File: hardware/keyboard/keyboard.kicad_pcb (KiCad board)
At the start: 2 copper layers, 234.9 x 95.7 mm, 82 parts, among them J1 Conn_01x02_Female, J2 Conn_01x03_Female, Q1 Q_NMOS_SGD, SW1 SW_Push, U1 SC0915, U10 CherryMX_LED, U11 CherryMX_LED, U12 CherryMX_LED, U13 CherryMX_LED, U14 CherryMX_LED, U15 CherryMX_LED, U16 CherryMX_LED, U17 CherryMX_LED, U18 CherryMX_LED, U19 CherryMX_LED, U2 MCP23008-xP, U20 CherryMX_LED, U21 CherryMX_LED, U22 CherryMX_LED, U23 CherryMX_LED, U24 CherryMX_LED, U25 CherryMX_LED, U26 CherryMX_LED, U27 CherryMX_LED, U28 CherryMX_LED, U29 CherryMX_LED, U3 CherryMX_LED, U30 CherryMX_LED, U31 CherryMX_LED, U32 CherryMX_LED, U33 CherryMX_LED, U34 CherryMX_LED, U35 CherryMX_LED, U36 CherryMX_LED, U4 CherryMX_LED, U5 CherryMX_LED, U6 CherryMX_LED, U7 CherryMX_LED, U8 CherryMX_LED, U9 CherryMX_LED

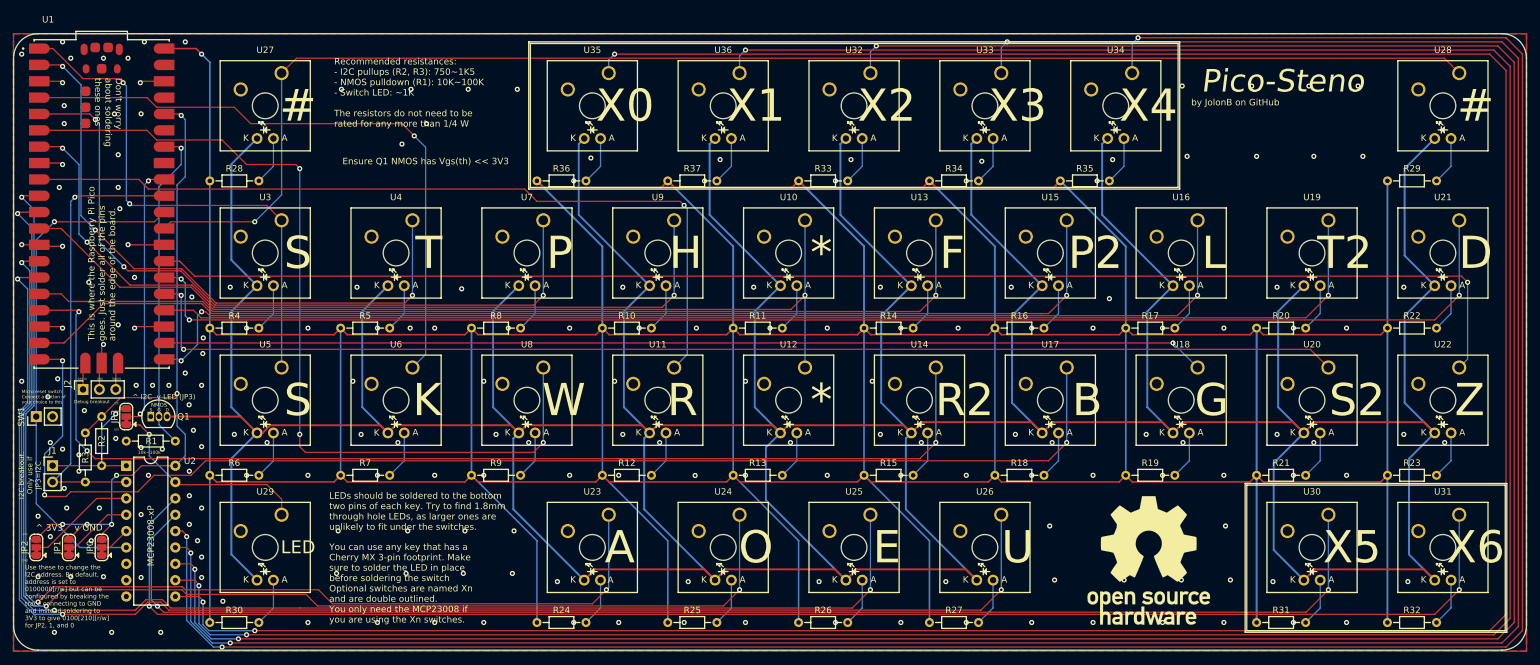
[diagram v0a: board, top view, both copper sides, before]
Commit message: Update I2C header
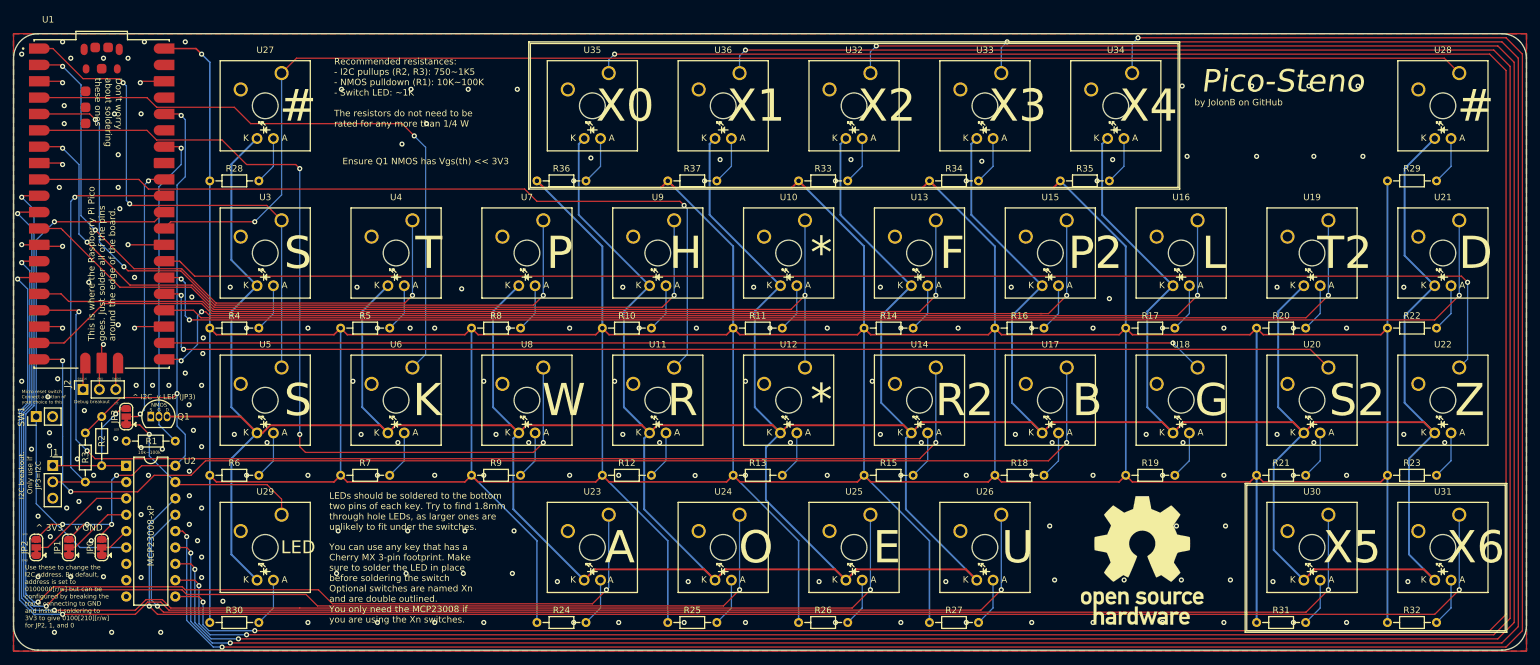
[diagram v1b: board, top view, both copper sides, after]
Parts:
- J1: value Conn_01x02_Female -> Conn_01x03_Female; footprint Connector_PinHeader_2.54mm:PinHeader_1x02_P2.54mm_Vertical -> Connector_PinSocket_2.54mm:PinSocket_1x03_P2.54mm_Vertical
- moved REF** 1.02 mm to (251.5, 215.1)
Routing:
- net /KEY_B: track 199.7 -> 194.1 mm
- net GND: vias 206 -> 207

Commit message: Add mounting holes
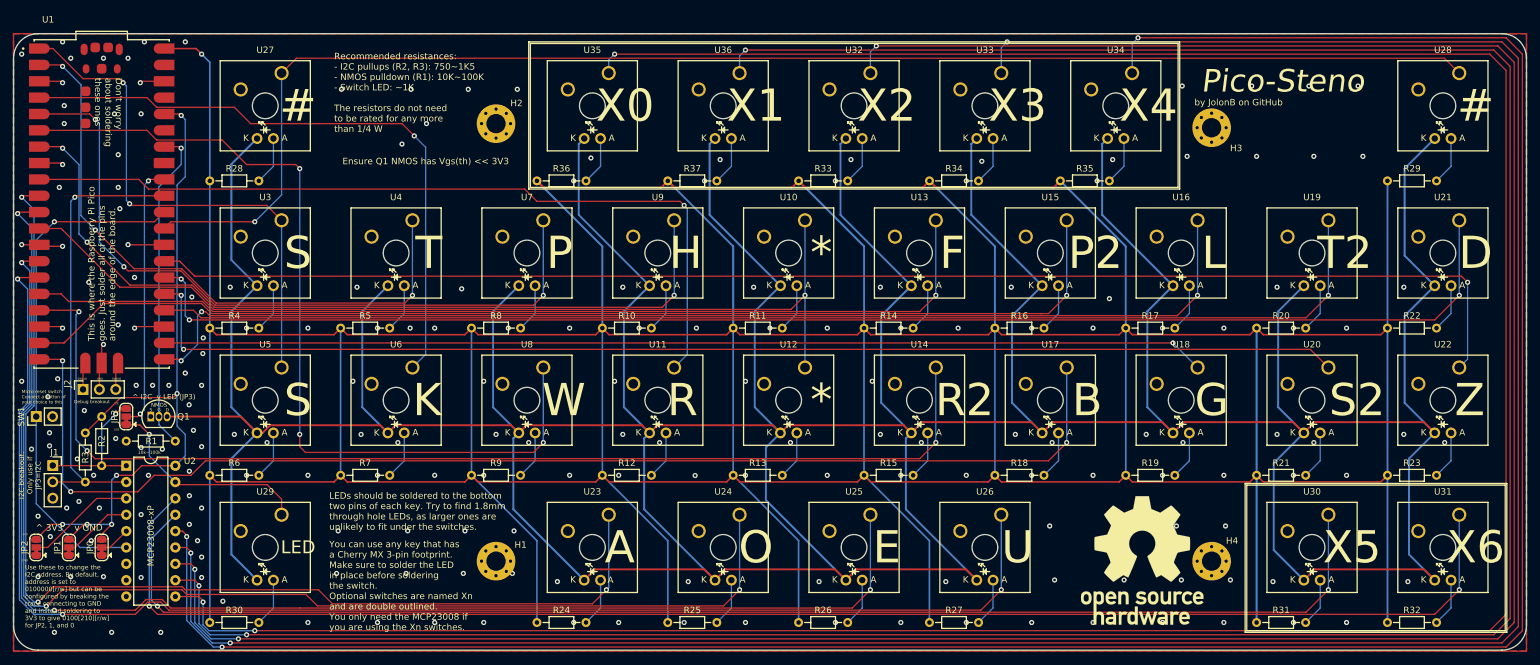
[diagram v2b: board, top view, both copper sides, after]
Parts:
- added H1: MountingHole_Pad, MountingHole:MountingHole_3mm_Pad_Via, F.Cu at (151.1, 215.3)
- added H2: MountingHole_Pad, MountingHole:MountingHole_3mm_Pad_Via, F.Cu at (151.1, 147.3)
- added H3: MountingHole_Pad, MountingHole:MountingHole_3mm_Pad_Via, F.Cu at (262.3, 148.0)
- added H4: MountingHole_Pad, MountingHole:MountingHole_3mm_Pad_Via, F.Cu at (262.3, 215.3)
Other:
- board text added: "You can use any key that has a Cherry MX 3-pin footprint. Make sure to solder the LED in place before soldering the switch. Optional switches are named Xn and are double outlined. You only need the MCP23008 if you are using the Xn switches."
- board text removed: "You can use any key that has a Cherry MX 3-pin footprint. Make sure to solder the LED in place before soldering the switch Optional switches are named Xn and are double outlined. You only need the MCP23008 if you are using the Xn switches."

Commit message: Add KiCad logo to PCB
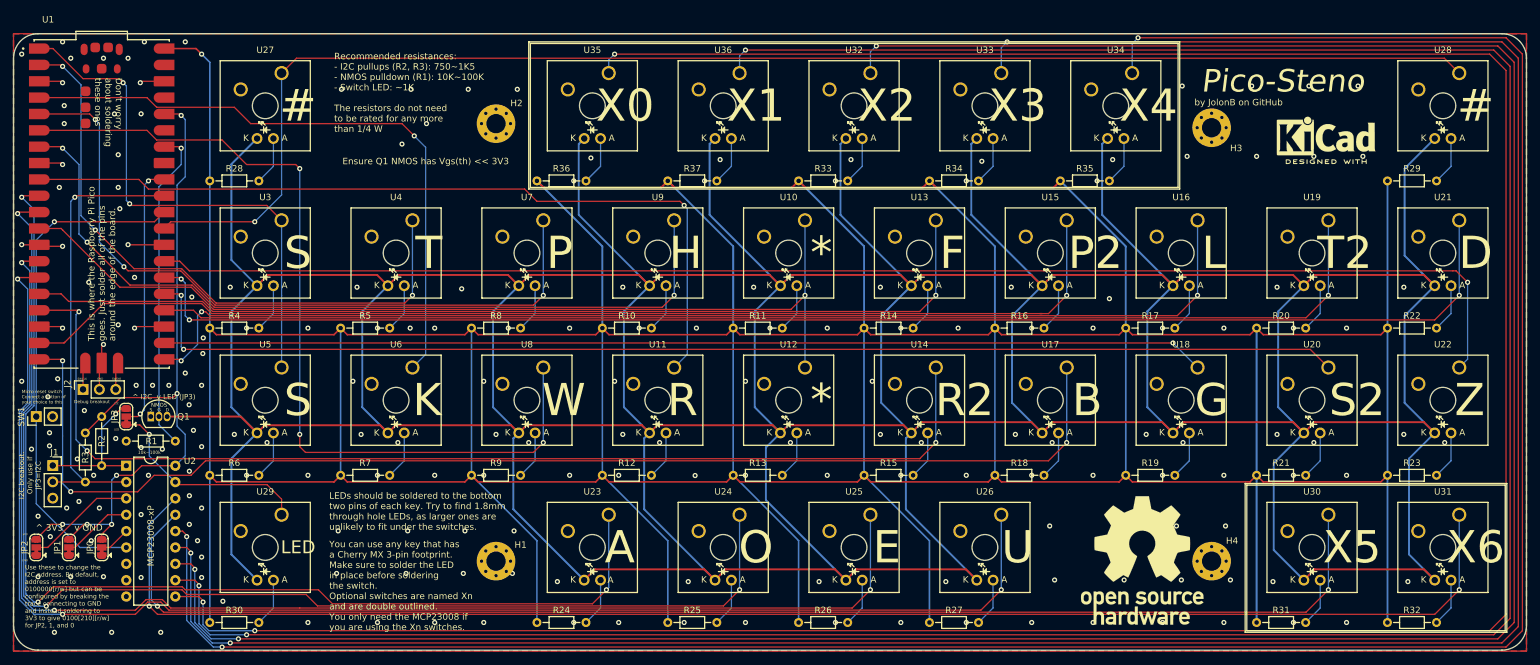
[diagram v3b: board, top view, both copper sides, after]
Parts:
- added REF**: KiCad-Logo2_6mm_SilkScreen, Symbol:KiCad-Logo2_6mm_SilkScreen, F.Cu at (280.0, 149.2)
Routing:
- net /LED_CTRL: track 941.7 -> 1137.0 mm
